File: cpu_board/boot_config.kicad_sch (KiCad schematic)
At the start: 30 parts, among them SW1 SW_DIP_x10, SW2 SW_DIP_x04

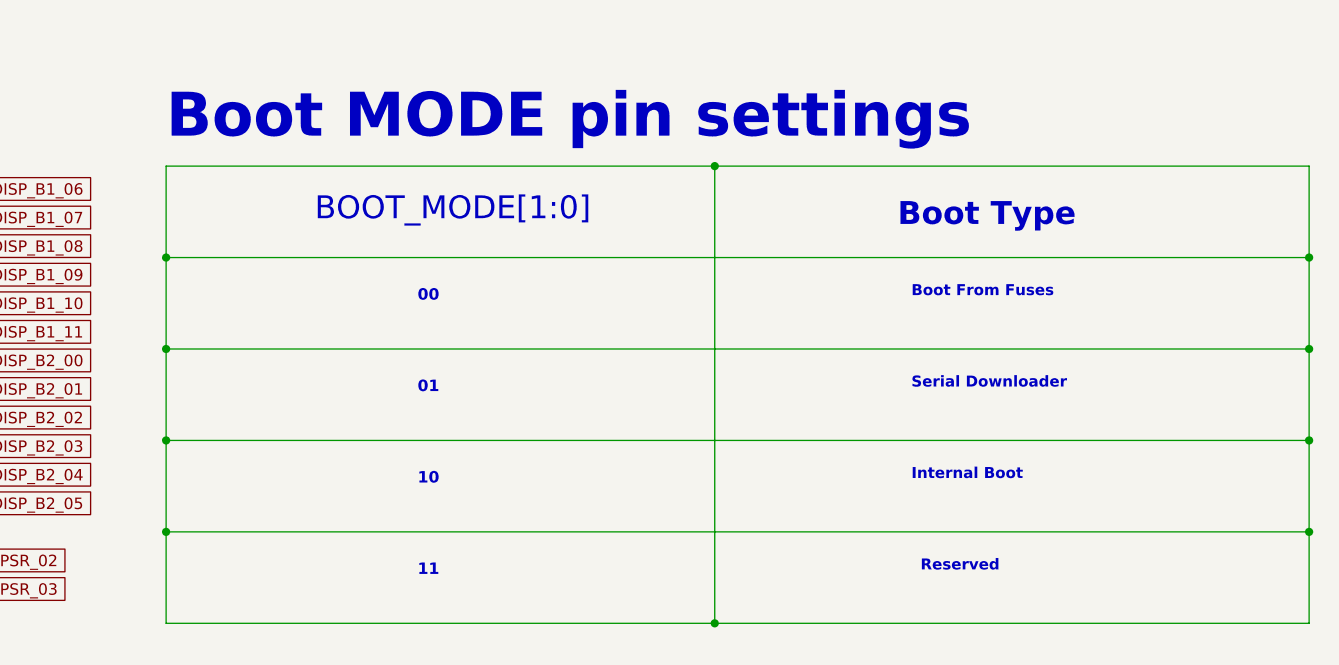
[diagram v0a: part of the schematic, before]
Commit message: clean up board2board connector and organize TODOs
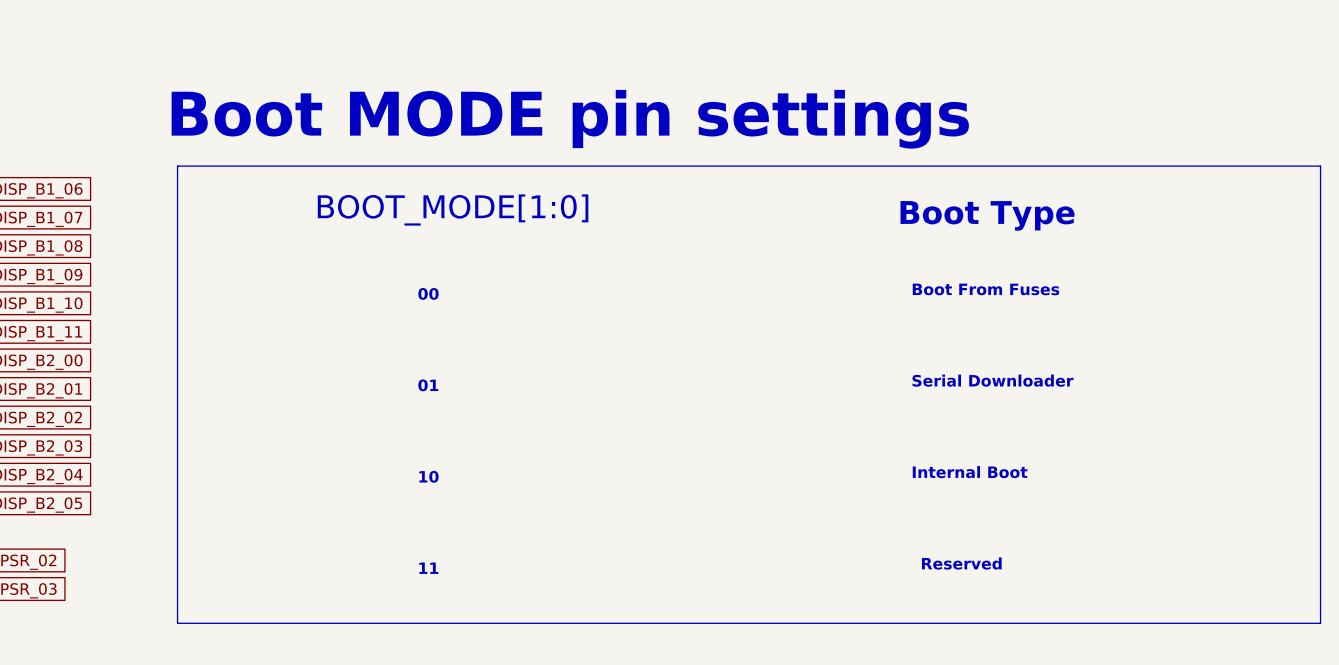
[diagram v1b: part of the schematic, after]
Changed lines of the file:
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@@
   (junction (at 114.935 83.82) (diameter 0) (color 0 0 0 0)
   )
-  (junction (at 220.98 134.62) (diameter 0) (color 0 0 0 0)
-  )
   (junction (at 90.17 171.45) (diameter 0) (color 0 0 0 0)
   )
@@
   (junction (at 90.17 168.275) (diameter 0) (color 0 0 0 0)
   )
-  (junction (at 220.98 154.94) (diameter 0) (color 0 0 0 0)
-  )
   (junction (at 155.575 83.82) (diameter 0) (color 0 0 0 0)
   )
-  (junction (at 220.98 144.78) (diameter 0) (color 0 0 0 0)
-  )
   (junction (at 125.095 146.05) (diameter 0) (color 0 0 0 0)
   )
@@
   (junction (at 90.17 133.35) (diameter 0) (color 0 0 0 0)
   )
-  (junction (at 220.98 165.1) (diameter 0) (color 0 0 0 0)
-  )
-  (junction (at 347.98 134.62) (diameter 0) (color 0 0 0 0)
-  )
   (junction (at 130.175 152.4) (diameter 0) (color 0 0 0 0)
   )
@@
   (junction (at 114.935 133.35) (diameter 0) (color 0 0 0 0)
   )
-  (junction (at 347.98 165.1) (diameter 0) (color 0 0 0 0)
-  )
-  (junction (at 347.98 144.78) (diameter 0) (color 0 0 0 0)
-  )
   (junction (at 117.475 83.82) (diameter 0) (color 0 0 0 0)
   )
   (junction (at 112.395 130.175) (diameter 0) (color 0 0 0 0)
   )
-  (junction (at 281.94 175.26) (diameter 0) (color 0 0 0 0)
-  )
   (junction (at 90.17 146.05) (diameter 0) (color 0 0 0 0)
   )
   (junction (at 117.475 136.525) (diameter 0) (color 0 0 0 0)
   )
-  (junction (at 347.98 154.94) (diameter 0) (color 0 0 0 0)
-  )
-  (junction (at 281.94 124.46) (diameter 0) (color 0 0 0 0)
-  )
   (junction (at 153.035 161.925) (diameter 0) (color 0 0 0 0)
   )
@@
     (stroke (width 0) (type default))
   )
-  (wire (pts (xy 220.98 124.46) (xy 281.94 124.46))
-    (stroke (width 0) (type default))
-  )
-  (wire (pts (xy 281.94 124.46) (xy 347.98 124.46))
-    (stroke (width 0) (type default))
-  )
   (wire (pts (xy 112.395 83.82) (xy 114.935 83.82))
     (stroke (width 0) (type default))
   )
-  (wire (pts (xy 347.98 134.62) (xy 347.98 144.78))
-    (stroke (width 0) (type default))
-  )
-  (wire (pts (xy 347.98 124.46) (xy 347.98 134.62))
-    (stroke (width 0) (type default))
-  )
   (wire (pts (xy 90.17 146.05) (xy 90.17 149.225))
     (stroke (width 0) (type default))
@@
     (stroke (width 0) (type default))
   )
-  (wire (pts (xy 220.98 134.62) (xy 347.98 134.62))
-    (stroke (width 0) (type default))
-  )
-  (wire (pts (xy 220.98 175.26) (xy 281.94 175.26))
-    (stroke (width 0) (type default))
-  )
   (wire (pts (xy 95.25 155.575) (xy 132.715 155.575))
     (stroke (width 0) (type default))
@@
     (stroke (width 0) (type default))
   )
-  (wire (pts (xy 220.98 154.94) (xy 347.98 154.94))
-    (stroke (width 0) (type default))
-  )
   (wire (pts (xy 95.25 171.45) (xy 155.575 171.45))
     (stroke (width 0) (type default))
@@
     (stroke (width 0) (type default))
   )
-  (wire (pts (xy 220.98 154.94) (xy 220.98 165.1))
-    (stroke (width 0) (type default))
-  )
-  (wire (pts (xy 220.98 165.1) (xy 220.98 175.26))
-    (stroke (width 0) (type default))
-  )
   (wire (pts (xy 95.25 142.875) (xy 122.555 142.875))
     (stroke (width 0) (type default))
@@
     (stroke (width 0) (type default))
   )
-  (wire (pts (xy 281.94 175.26) (xy 347.98 175.26))
-    (stroke (width 0) (type default))
-  )
   (wire (pts (xy 90.17 139.7) (xy 90.17 142.875))
     (stroke (width 0) (type default))
@@
     (stroke (width 0) (type default))
   )
-  (wire (pts (xy 220.98 124.46) (xy 220.98 134.62))
-    (stroke (width 0) (type default))
-  )
   (wire (pts (xy 158.115 78.105) (xy 158.115 83.82))
     (stroke (width 0) (type default))
@@
     (stroke (width 0) (type default))
   )
-  (wire (pts (xy 220.98 165.1) (xy 347.98 165.1))
-    (stroke (width 0) (type default))
-  )
   (wire (pts (xy 180.975 142.875) (xy 194.945 142.875))
     (stroke (width 0) (type default))
@@
     (stroke (width 0) (type default))
   )
-  (wire (pts (xy 220.98 144.78) (xy 220.98 154.94))
-    (stroke (width 0) (type default))
-  )
   (wire (pts (xy 127.635 149.225) (xy 175.895 149.225))
     (stroke (width 0) (type default))
@@
     (stroke (width 0) (type default))
   )
-  (wire (pts (xy 347.98 144.78) (xy 347.98 154.94))
-    (stroke (width 0) (type default))
-  )
   (wire (pts (xy 127.635 99.06) (xy 127.635 149.225))
     (stroke (width 0) (type default))
@@
     (stroke (width 0) (type default))
   )
-  (wire (pts (xy 281.94 124.46) (xy 281.94 175.26))
-    (stroke (width 0) (type default))
-  )
   (wire (pts (xy 90.17 158.75) (xy 90.17 161.925))
     (stroke (width 0) (type default))
@@
     (stroke (width 0) (type default))
   )
-  (wire (pts (xy 220.98 134.62) (xy 220.98 144.78))
-    (stroke (width 0) (type default))
-  )
   (wire (pts (xy 117.475 99.06) (xy 117.475 136.525))
     (stroke (width 0) (type default))
@@
     (stroke (width 0) (type default))
   )
-  (wire (pts (xy 347.98 154.94) (xy 347.98 165.1))
-    (stroke (width 0) (type default))
-  )
   (wire (pts (xy 95.25 139.7) (xy 120.015 139.7))
     (stroke (width 0) (type default))
@@
     (stroke (width 0) (type default))
   )
-  (wire (pts (xy 220.98 144.78) (xy 347.98 144.78))
-    (stroke (width 0) (type default))
-  )
   (wire (pts (xy 180.975 130.175) (xy 194.945 130.175))
     (stroke (width 0) (type default))
@@
     (stroke (width 0) (type default))
   )
-  (wire (pts (xy 347.98 165.1) (xy 347.98 175.26))
-    (stroke (width 0) (type default))
-  )
   (wire (pts (xy 90.17 161.925) (xy 90.17 168.275))
     (stroke (width 0) (type default))
@@
     (stroke (width 0) (type default))
   )
+  (rectangle (start 222.25 124.46) (end 349.25 175.26)
+    (stroke (width 0) (type default))
+    (fill (type none))
+  )
   (text "BOOT_MODE[1]" (at 136.525 171.45 0)
     (effects (font (size 1.27 1.27)) (justify left bottom))
   )
   (text "Internal Boot" (at 303.784 159.512 0)
-    (effects (font (size 1.2192 1.2192) (thickness 0.2438) bold) (justify left bottom))
+    (effects (font (size 1.27 1.27) (thickness 0.2438) bold) (justify left bottom))
   )
   (text "11" (at 248.92 170.18 0)
@@
   )
   (text "Serial Downloader" (at 303.784 149.352 0)
-    (effects (font (size 1.2192 1.2192) (thickness 0.2438) bold) (justify left bottom))
+    (effects (font (size 1.27 1.27) (thickness 0.2438) bold) (justify left bottom))
   )
   (text "BT_CFG[2]" (at 136.525 133.35 0)
@@
   )
   (text "Boot From Fuses" (at 303.784 139.192 0)
-    (effects (font (size 1.2192 1.2192) (thickness 0.2438) bold) (justify left bottom))
+    (effects (font (size 1.27 1.27) (thickness 0.2438) bold) (justify left bottom))
   )
   (text "BT_CFG[1]" (at 136.525 130.175 0)
@@
   )
   (text "Reserved" (at 304.8 169.672 0)
-    (effects (font (size 1.2192 1.2192) (thickness 0.2438) bold) (justify left bottom))
+    (effects (font (size 1.27 1.27) (thickness 0.2438) bold) (justify left bottom))
   )
   (text "BT_CFG[0]" (at 136.525 127 0)

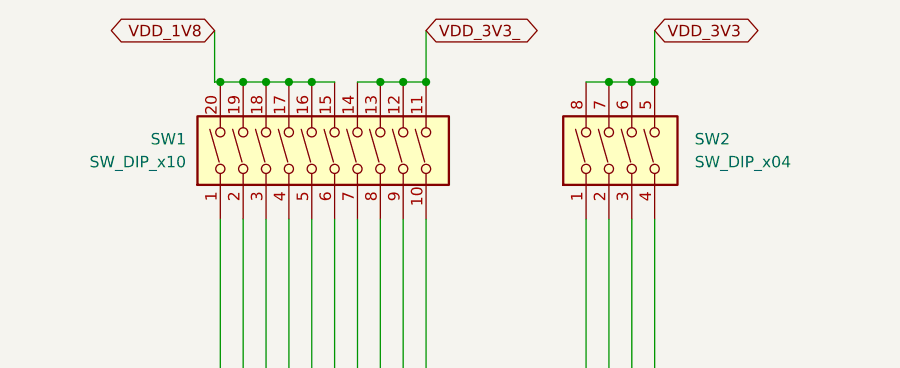
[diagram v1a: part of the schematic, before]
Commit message: route most of power distribution
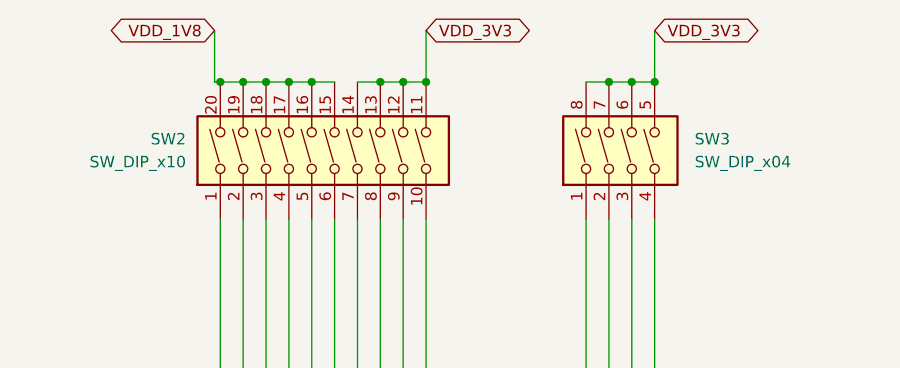
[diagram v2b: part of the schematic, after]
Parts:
- renumbered SW1 to SW2, SW2 to SW3
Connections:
- net VDD_3V3_ is gone; now on net VDD_3V3: SW2.11, SW2.12, SW2.13, SW2.14

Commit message: continue work on fanout
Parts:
- R? (x28): footprint Resistor_SMD:R_0402_1005Metric -> adcs:Perfect_0402
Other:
- note added: "DOUBLE CHECK LOGIC LEVELS"
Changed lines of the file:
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@@
     (effects (font (size 1.27 1.27) (thickness 0.3048) bold) (justify left bottom))
+  )
+  (text "DOUBLE CHECK LOGIC LEVELS\n" (at 114.935 61.595 0)
+    (effects (font (size 5 5) (thickness 1) bold (color 194 0 0 1)) (justify left bottom))
   )
   (text "BT_CFG[10]" (at 136.525 158.75 0)
@@
       (effects (font (size 1.27 1.27)))
     )
-    (property "Footprint" "Resistor_SMD:R_0402_1005Metric" (at 92.71 127 0)
+    (property "Footprint" "adcs:Perfect_0402" (at 92.71 127 0)
       (effects (font (size 1.27 1.27)) hide)
     )
@@
       (effects (font (size 1.27 1.27)))
     )
-    (property "Footprint" "Resistor_SMD:R_0402_1005Metric" (at 178.435 168.275 0)
+    (property "Footprint" "adcs:Perfect_0402" (at 178.435 168.275 0)
       (effects (font (size 1.27 1.27)) hide)
     )
@@
       (effects (font (size 1.27 1.27)))
     )
-    (property "Footprint" "Resistor_SMD:R_0402_1005Metric" (at 178.435 158.75 0)
+    (property "Footprint" "adcs:Perfect_0402" (at 178.435 158.75 0)
       (effects (font (size 1.27 1.27)) hide)
     )
@@
       (effects (font (size 1.27 1.27)))
     )
-    (property "Footprint" "Resistor_SMD:R_0402_1005Metric" (at 92.71 136.525 0)
+    (property "Footprint" "adcs:Perfect_0402" (at 92.71 136.525 0)
       (effects (font (size 1.27 1.27)) hide)
     )
@@
       (effects (font (size 1.27 1.27)))
     )
-    (property "Footprint" "Resistor_SMD:R_0402_1005Metric" (at 92.71 133.35 0)
+    (property "Footprint" "adcs:Perfect_0402" (at 92.71 133.35 0)
       (effects (font (size 1.27 1.27)) hide)
     )
@@
       (effects (font (size 1.27 1.27)))
     )
-    (property "Footprint" "Resistor_SMD:R_0402_1005Metric" (at 178.435 152.4 0)
+    (property "Footprint" "adcs:Perfect_0402" (at 178.435 152.4 0)
       (effects (font (size 1.27 1.27)) hide)
     )
@@
       (effects (font (size 1.27 1.27)))
     )
-    (property "Footprint" "Resistor_SMD:R_0402_1005Metric" (at 178.435 155.575 0)
+    (property "Footprint" "adcs:Perfect_0402" (at 178.435 155.575 0)
       (effects (font (size 1.27 1.27)) hide)
     )
@@
       (effects (font (size 1.27 1.27)))
     )
-    (property "Footprint" "Resistor_SMD:R_0402_1005Metric" (at 92.71 146.05 0)
+    (property "Footprint" "adcs:Perfect_0402" (at 92.71 146.05 0)
       (effects (font (size 1.27 1.27)) hide)
     )
@@
       (effects (font (size 1.27 1.27)))
     )
-    (property "Footprint" "Resistor_SMD:R_0402_1005Metric" (at 92.71 161.925 0)
+    (property "Footprint" "adcs:Perfect_0402" (at 92.71 161.925 0)
       (effects (font (size 1.27 1.27)) hide)
     )
@@
       (effects (font (size 1.27 1.27)))
     )
-    (property "Footprint" "Resistor_SMD:R_0402_1005Metric" (at 178.435 136.525 0)
+    (property "Footprint" "adcs:Perfect_0402" (at 178.435 136.525 0)
       (effects (font (size 1.27 1.27)) hide)
     )
@@
       (effects (font (size 1.27 1.27)))
     )
-    (property "Footprint" "Resistor_SMD:R_0402_1005Metric" (at 178.435 130.175 0)
+    (property "Footprint" "adcs:Perfect_0402" (at 178.435 130.175 0)
       (effects (font (size 1.27 1.27)) hide)
     )
@@
       (effects (font (size 1.27 1.27)))
     )
-    (property "Footprint" "Resistor_SMD:R_0402_1005Metric" (at 92.71 139.7 0)
+    (property "Footprint" "adcs:Perfect_0402" (at 92.71 139.7 0)
       (effects (font (size 1.27 1.27)) hide)
     )
@@
       (effects (font (size 1.27 1.27)))
     )
-    (property "Footprint" "Resistor_SMD:R_0402_1005Metric" (at 92.71 168.275 0)
+    (property "Footprint" "adcs:Perfect_0402" (at 92.71 168.275 0)
       (effects (font (size 1.27 1.27)) hide)
     )
@@
       (effects (font (size 1.27 1.27)))
     )
-    (property "Footprint" "Resistor_SMD:R_0402_1005Metric" (at 178.435 133.35 0)
+    (property "Footprint" "adcs:Perfect_0402" (at 178.435 133.35 0)
       (effects (font (size 1.27 1.27)) hide)
     )
@@
       (effects (font (size 1.27 1.27)))
     )
-    (property "Footprint" "Resistor_SMD:R_0402_1005Metric" (at 92.71 152.4 0)
+    (property "Footprint" "adcs:Perfect_0402" (at 92.71 152.4 0)
       (effects (font (size 1.27 1.27)) hide)
     )
@@
       (effects (font (size 1.27 1.27)))
     )
-    (property "Footprint" "Resistor_SMD:R_0402_1005Metric" (at 178.435 149.225 0)
+    (property "Footprint" "adcs:Perfect_0402" (at 178.435 149.225 0)
       (effects (font (size 1.27 1.27)) hide)
     )
@@
       (effects (font (size 1.27 1.27)))
     )
-    (property "Footprint" "Resistor_SMD:R_0402_1005Metric" (at 178.435 139.7 0)
+    (property "Footprint" "adcs:Perfect_0402" (at 178.435 139.7 0)
       (effects (font (size 1.27 1.27)) hide)
     )
@@
       (effects (font (size 1.27 1.27)))
     )
-    (property "Footprint" "Resistor_SMD:R_0402_1005Metric" (at 92.71 158.75 0)
+    (property "Footprint" "adcs:Perfect_0402" (at 92.71 158.75 0)
       (effects (font (size 1.27 1.27)) hide)
     )
@@
       (effects (font (size 1.27 1.27)))
     )
-    (property "Footprint" "Resistor_SMD:R_0402_1005Metric" (at 178.435 146.05 0)
+    (property "Footprint" "adcs:Perfect_0402" (at 178.435 146.05 0)
       (effects (font (size 1.27 1.27)) hide)
     )
@@
       (effects (font (size 1.27 1.27)))
     )
-    (property "Footprint" "Resistor_SMD:R_0402_1005Metric" (at 178.435 161.925 0)
+    (property "Footprint" "adcs:Perfect_0402" (at 178.435 161.925 0)
       (effects (font (size 1.27 1.27)) hide)
     )
@@
       (effects (font (size 1.27 1.27)))
     )
-    (property "Footprint" "Resistor_SMD:R_0402_1005Metric" (at 178.435 171.45 0)
+    (property "Footprint" "adcs:Perfect_0402" (at 178.435 171.45 0)
       (effects (font (size 1.27 1.27)) hide)
     )
@@
       (effects (font (size 1.27 1.27)))
     )
-    (property "Footprint" "Resistor_SMD:R_0402_1005Metric" (at 92.71 149.225 0)
+    (property "Footprint" "adcs:Perfect_0402" (at 92.71 149.225 0)
       (effects (font (size 1.27 1.27)) hide)
     )
@@
       (effects (font (size 1.27 1.27)))
     )
-    (property "Footprint" "Resistor_SMD:R_0402_1005Metric" (at 178.435 142.875 0)
+    (property "Footprint" "adcs:Perfect_0402" (at 178.435 142.875 0)
       (effects (font (size 1.27 1.27)) hide)
     )
@@
       (effects (font (size 1.27 1.27)))
     )
-    (property "Footprint" "Resistor_SMD:R_0402_1005Metric" (at 178.435 127 0)
+    (property "Footprint" "adcs:Perfect_0402" (at 178.435 127 0)
       (effects (font (size 1.27 1.27)) hide)
     )
@@
       (effects (font (size 1.27 1.27)))
     )
-    (property "Footprint" "Resistor_SMD:R_0402_1005Metric" (at 92.71 130.175 0)
+    (property "Footprint" "adcs:Perfect_0402" (at 92.71 130.175 0)
       (effects (font (size 1.27 1.27)) hide)
     )
@@
       (effects (font (size 1.27 1.27)))
     )
-    (property "Footprint" "Resistor_SMD:R_0402_1005Metric" (at 92.71 142.875 0)
+    (property "Footprint" "adcs:Perfect_0402" (at 92.71 142.875 0)
       (effects (font (size 1.27 1.27)) hide)
     )
@@
       (effects (font (size 1.27 1.27)))
     )
-    (property "Footprint" "Resistor_SMD:R_0402_1005Metric" (at 92.71 171.45 0)
+    (property "Footprint" "adcs:Perfect_0402" (at 92.71 171.45 0)
       (effects (font (size 1.27 1.27)) hide)
     )
@@
       (effects (font (size 1.27 1.27)))
     )
-    (property "Footprint" "Resistor_SMD:R_0402_1005Metric" (at 92.71 155.575 0)
-      (effects (font (size 1.27 1.27)) hide)
-    )
+    (property "Footprint" "adcs:Perfect_0402" (at 92.71 155.575 0)
+      (effects (font (size 1.27 1.27)) hide)
+    )

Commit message: update
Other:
- company: (none) -> Stanford Student Space Initiative
- title: (none) -> Soldermander
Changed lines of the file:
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@@
 (kicad_sch (version 20230121) (generator eeschema)
   (paper "A3")
+  (title_block
+    (title "Soldermander")
+    (date "2024-02-27")
+    (rev "1.0")
+    (company "Stanford Student Space Initiative")
+    (comment 1 "RE: Flynn Dreilinger")
+  )
   (junction (at 114.935 83.82) (diameter 0) (color 0 0 0 0)
   )
